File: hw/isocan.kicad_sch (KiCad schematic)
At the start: 10 parts, among them U13 XC6206P332MR, U6 ADUM1201ARZ-RL7, U9 TJA1051TK/3,118

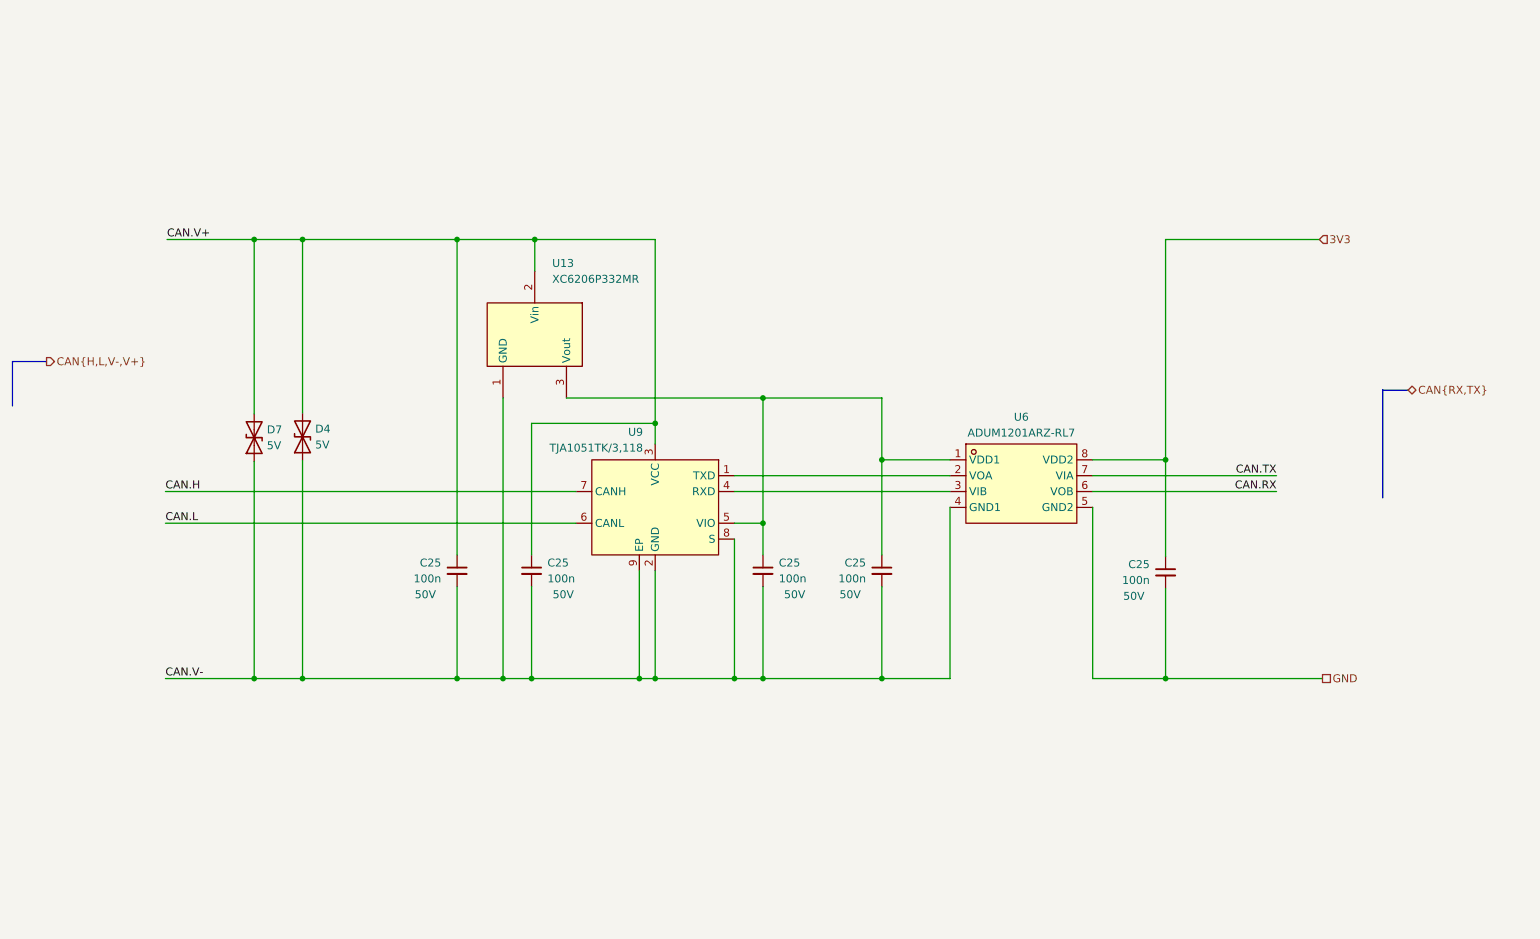
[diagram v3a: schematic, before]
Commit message: [Hw] Simplifying CAN
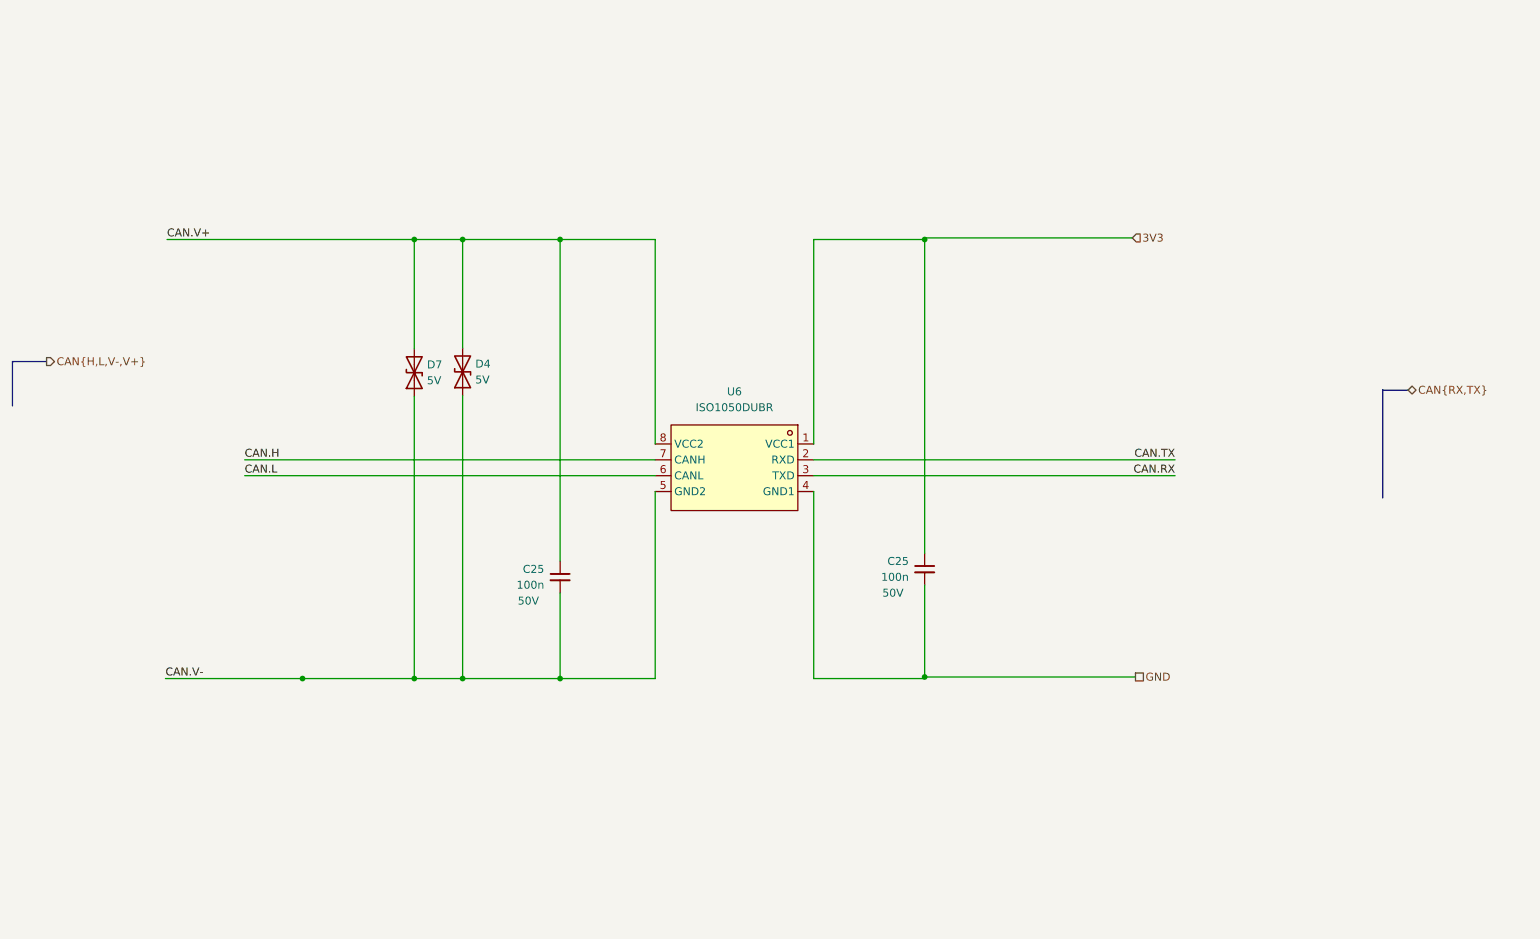
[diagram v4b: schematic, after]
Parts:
- removed C25 (x3): 100n, Capacitor_SMD:C_0402_1005Metric, symbol Device:C_Small
- removed U13: XC6206P332MR, easyeda:SOT-23-3_L2.9-W1.6-P1.90-LS2.8-BR, symbol easyeda:XC6206P332MR
- removed U6: ADUM1201ARZ-RL7, easyeda:SOIC-8_L4.9-W3.9-P1.27-LS6.0-BL, symbol easyeda:ADUM1201ARZ-RL7
- removed U9: TJA1051TK/3,118, easyeda:HVSON-8_L3.0-W3.0-P0.65-BL-EP, symbol easyeda:TJA1051TK_3,118
- added U6: ISO1050DUBR, easyeda:SOIC-8_L9.3-W6.6-P2.54-LS10.4-BL, symbol easyeda:ISO1050DUBR
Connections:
- net 3V3: now also U6.1 (VCC1)
- net CAN.H: now also U6.7 (CANH)
- net CAN.L: now also U6.6 (CANL)
- net CAN.RX: now also U6.3 (TXD)
- net CAN.TX: now also U6.2 (RXD)
- net CAN.V+: now also U6.8 (VCC2)
- net CAN.V-: now also U6.5 (GND2)
- net GND: now also U6.4 (GND1)
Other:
- moved on the sheet: C25, D4, D7

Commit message: [Hw] Small ICs to make 3 wire can possible in this formfactor
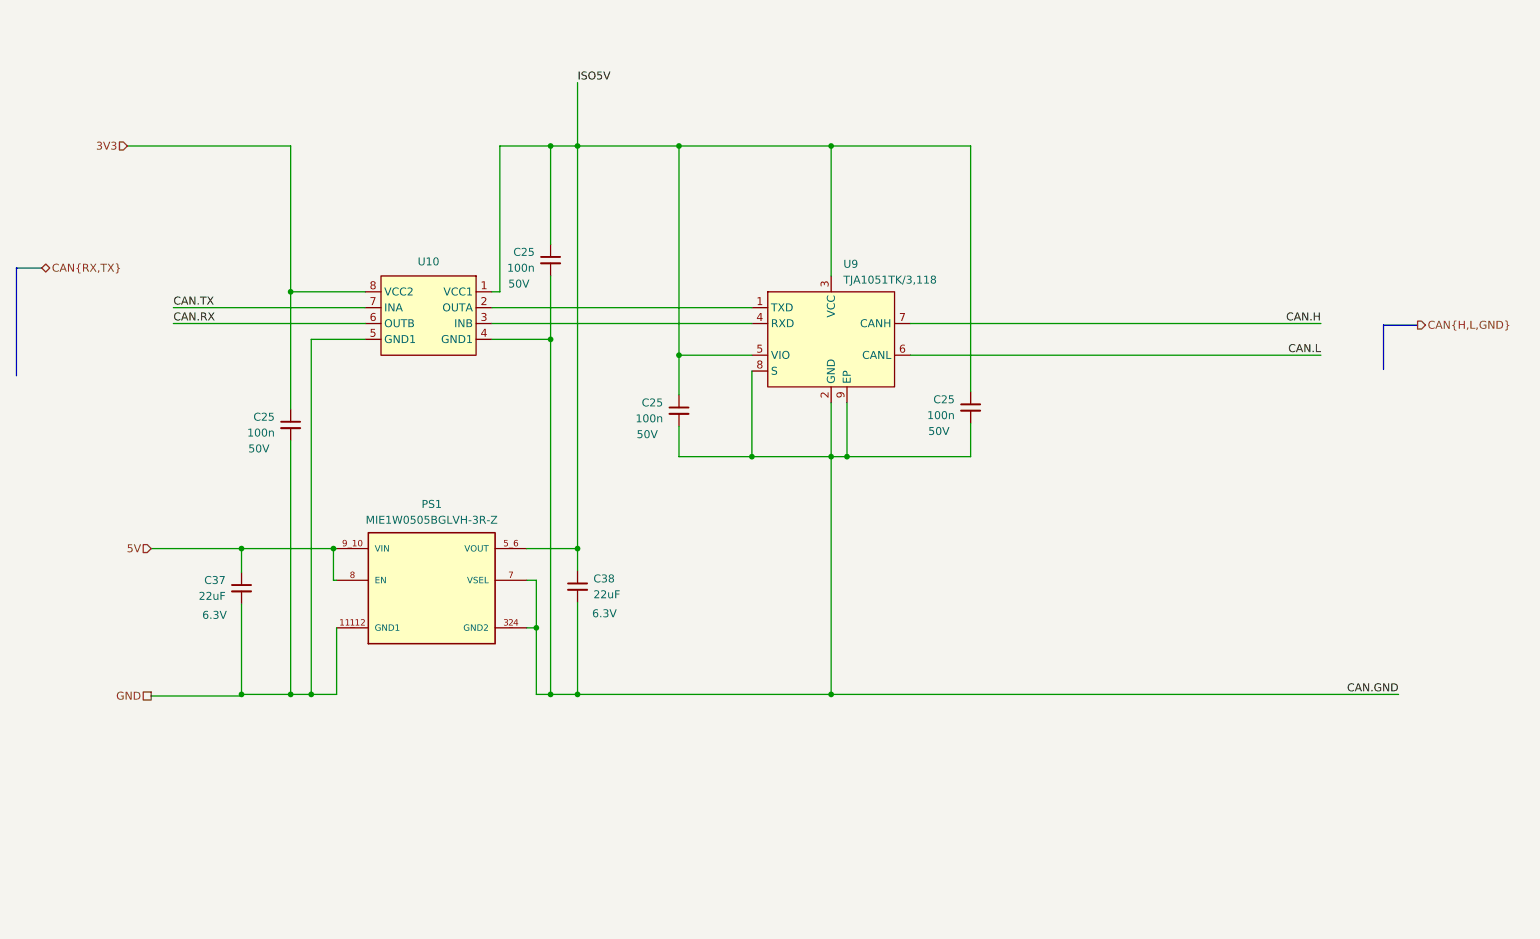
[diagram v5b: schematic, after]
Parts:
- removed C25: 100n, Capacitor_SMD:C_0402_1005Metric, symbol Device:C_Small
- removed D4, D7: 5V, easyeda:X1-DFN1006-2_L1.0-W0.6-RD, symbol Device:D_TVS
- removed U6: ISO1050DUBR, easyeda:SOIC-8_L9.3-W6.6-P2.54-LS10.4-BL, symbol easyeda:ISO1050DUBR
- added C25 (x3): 100n, Capacitor_SMD:C_0402_1005Metric, symbol Device:C_Small
- added C37, C38: 22uF, Capacitor_SMD:C_0402_1005Metric, symbol Device:C_Small
- added PS1: MIE1W0505BGLVH-3R-Z, MIE1W0505BGLVH-3R-Z:CONV_MIE1W0505BGLVH-3R-Z, symbol MIE1W0505BGLVH-3R-Z:MIE1W0505BGLVH-3R-Z
- added U10: ~, Package_DFN_QFN:DFN-8-1EP_3x2mm_P0.5mm_EP1.3x1.5mm, symbol local_lib:ISO6521FREUR
- added U9: TJA1051TK/3,118, easyeda:HVSON-8_L3.0-W3.0-P0.65-BL-EP, symbol easyeda:TJA1051TK_3,118
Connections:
- net 3V3: now also U10.8 (VCC2)
- net CAN.H: now also U9.7 (CANH)
- net CAN.L: now also U9.6 (CANL)
- net CAN.RX: now also U10.6 (OUTB)
- net CAN.TX: now also U10.7 (INA)
- net GND: now also C37.2, PS1.1 (GND1), PS1.11_12 (GND1), U10.5 (GND1)
- new net: U10.2 (OUTA), U9.1 (TXD)
- new net: U10.3 (INB), U9.4 (RXD)
- new net 5V: C37.1, PS1.8 (EN), PS1.9_10 (VIN)
- new net CAN.GND: C25.2, C25.2, C25.2, C38.2, PS1.2 (GND2), PS1.3_4 (GND2), PS1.7 (VSEL), U10.4 (GND1), U9.2 (GND), U9.8 (S), U9.9 (EP)
- new net ISO5V: C25.1, C25.1, C25.1, C38.1, PS1.5_6 (VOUT), U10.1 (VCC1), U9.3 (VCC), U9.5 (VIO)
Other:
- moved on the sheet: C25

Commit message: [Hw] USBC fixes, 3 wire can, encoder and comms headers
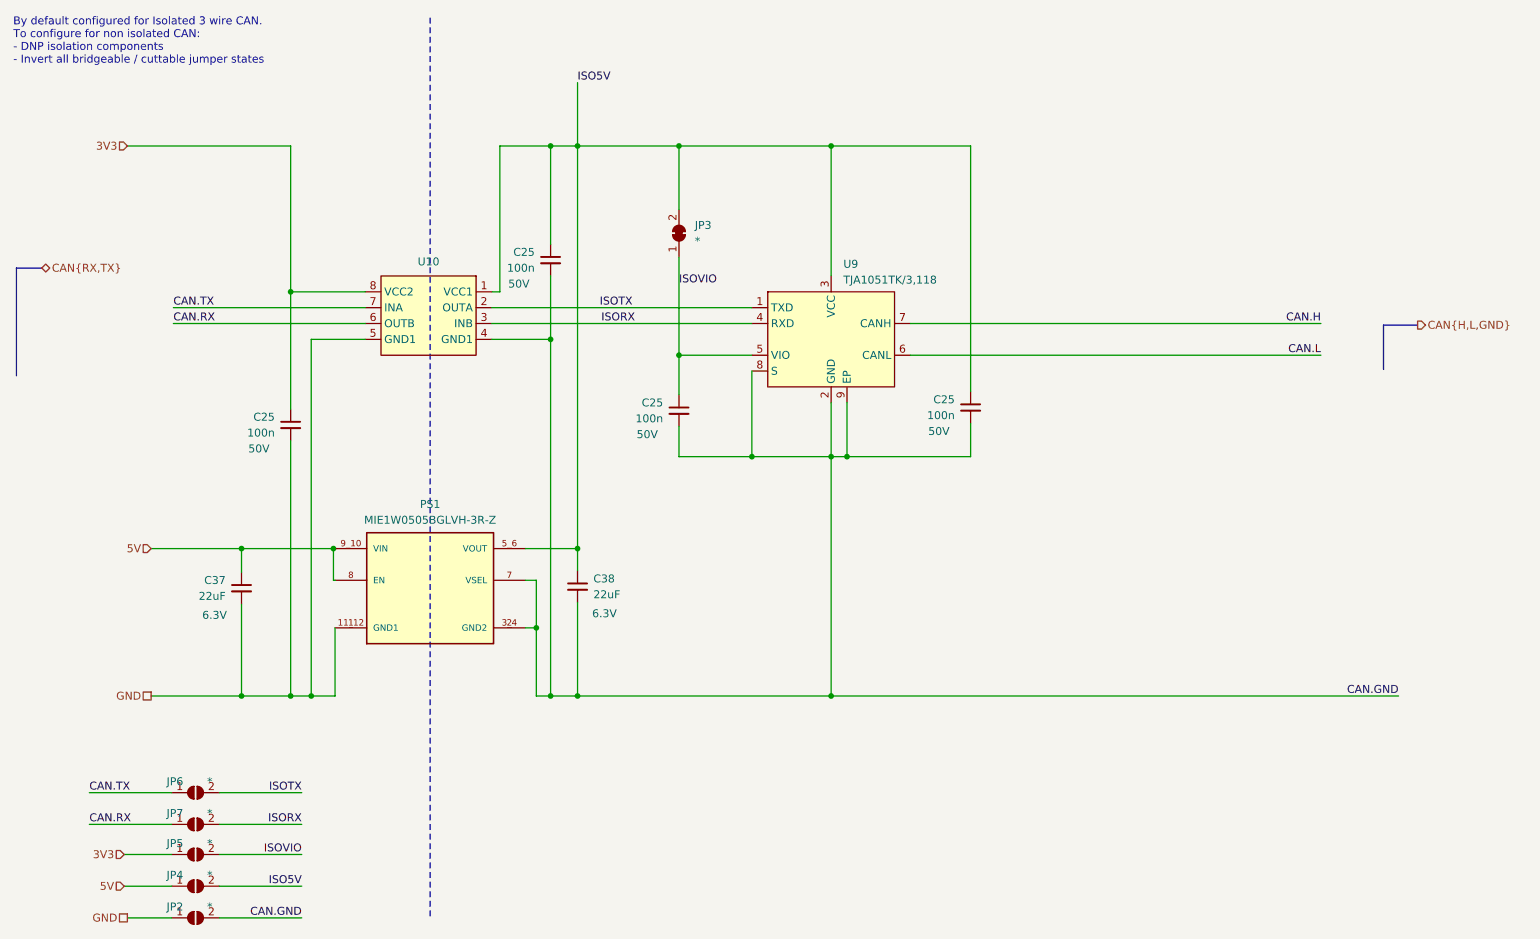
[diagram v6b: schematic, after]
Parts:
- added JP2, JP4, JP5, JP6, JP7: *, Jumper:SolderJumper-2_P1.3mm_Open_RoundedPad1.0x1.5mm, symbol Jumper:SolderJumper_2_Open
- added JP3: *, Jumper:SolderJumper-2_P1.3mm_Bridged_RoundedPad1.0x1.5mm, symbol Jumper:SolderJumper_2_Bridged
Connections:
- net 3V3: now also JP5.1 (A)
- net 5V: now also JP4.1 (A)
- net CAN.GND: now also JP2.2 (B)
- net CAN.RX: now also JP7.1 (A)
- net CAN.TX: now also JP6.1 (A)
- net GND: now also JP2.1 (A)
- net ISO5V: now also JP3.2 (B), JP4.2 (B); no longer C25.1, U9.5 (VIO)
- net ISOTX: now reaches U10.2 (OUTA), U9.1 (TXD)
- net ISOTX: now also JP6.2 (B)
- net ISORX: now reaches U10.3 (INB), U9.4 (RXD)
- net ISORX: now also JP7.2 (B)
- new net ISOVIO: C25.1, JP3.1 (A), JP5.2 (B), U9.5 (VIO)
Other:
- note added: "By default configured for Isolated 3 wire CAN. To configure for non isolated CAN: - DNP isolation components - Invert all bridgeable / cuttable jumper states"

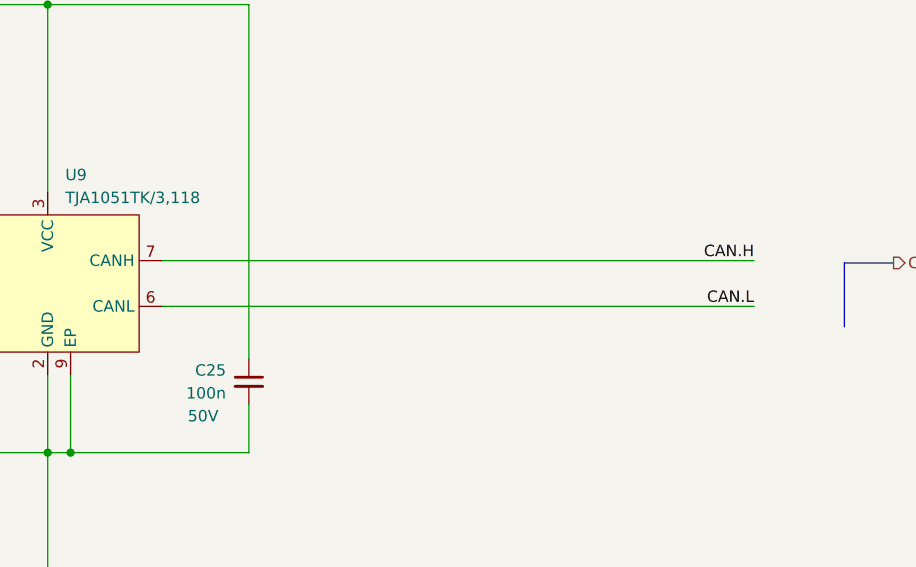
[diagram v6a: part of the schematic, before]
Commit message: [Hw] Optimised pin out for routing, new layout
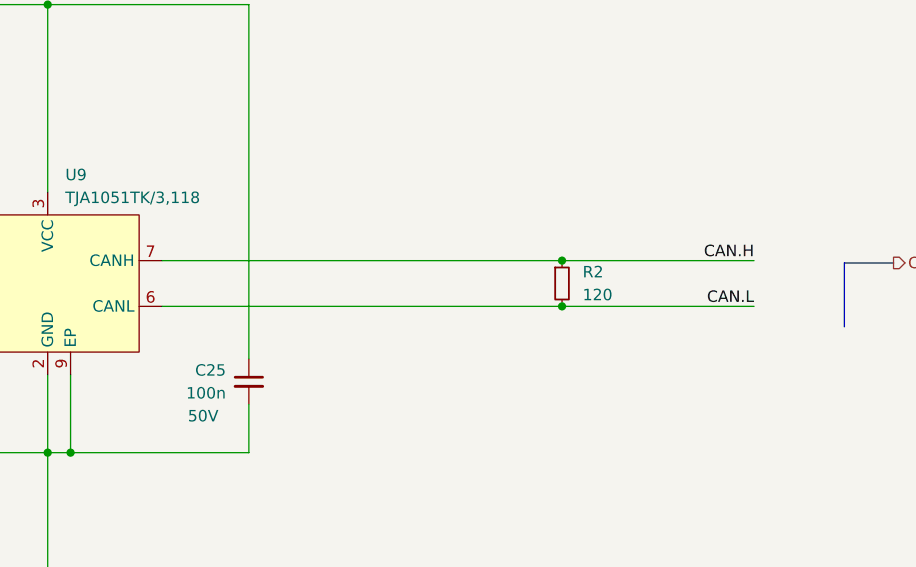
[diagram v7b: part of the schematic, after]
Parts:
- added R2: 120, Resistor_SMD:R_0603_1608Metric, symbol Device:R_Small
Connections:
- net CAN.H: now also R2.1
- net CAN.L: now also R2.2
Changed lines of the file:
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@@
   (junction (at 115.316 134.874) (diameter 0) (color 0 0 0 0)
   )
+  (junction (at 217.424 80.264) (diameter 0) (color 0 0 0 0)
+  )
   (junction (at 73.66 70.104) (diameter 0) (color 0 0 0 0)
   )
@@
   (junction (at 160.274 46.736) (diameter 0) (color 0 0 0 0)
   )
+  (junction (at 217.424 75.184) (diameter 0) (color 0 0 0 0)
+  )
   (junction (at 115.316 77.724) (diameter 0) (color 0 0 0 0)
   )
@@
     (stroke (width 0) (type default))
   )
-  (wire (pts (xy 238.76 75.184) (xy 172.974 75.184))
+  (wire (pts (xy 238.76 75.184) (xy 217.424 75.184))
     (stroke (width 0) (type default))
   )
@@
     (stroke (width 0) (type default))
   )
+  (wire (pts (xy 217.424 75.184) (xy 172.974 75.184))
+    (stroke (width 0) (type default))
+  )
   (wire (pts (xy 147.574 96.52) (xy 135.89 96.52))
     (stroke (width 0) (type default))
@@
     (stroke (width 0) (type default))
   )
+  (wire (pts (xy 217.424 80.264) (xy 172.974 80.264))
+    (stroke (width 0) (type default))
+  )
   (wire (pts (xy 105.918 77.724) (xy 115.316 77.724))
     (stroke (width 0) (type default))
@@
     (stroke (width 0) (type default))
   )
-  (wire (pts (xy 238.76 80.264) (xy 172.974 80.264))
+  (wire (pts (xy 238.76 80.264) (xy 217.424 80.264))
     (stroke (width 0) (type default))
   )
@@
         )
       )
+    )
+  )
+  (symbol (lib_id "Device:R_Small") (at 217.424 77.724 0) (unit 1)
+    (in_bom yes) (on_board yes) (dnp no) (fields_autoplaced)
+    (property "Reference" "R2" (at 219.71 76.454 0)
+      (effects (font (size 1.27 1.27)) (justify left))
+    )
+    (property "Value" "120" (at 219.71 78.994 0)
+      (effects (font (size 1.27 1.27)) (justify left))
+    )
+    (property "Footprint" "Resistor_SMD:R_0603_1608Metric" (at 217.424 77.724 0)
+      (effects (font (size 1.27 1.27)) hide)
+    )
+    (property "Datasheet" "~" (at 217.424 77.724 0)
+      (effects (font (size 1.27 1.27)) hide)
+    )
+    (pin "1")
+    (pin "2")
+    (instances
+      (project "foc8313"
+        (path "/6a0f293a-1ae1-497a-a3c1-0d8f9e6f81b9/67c38edc-7843-4b4c-b50a-94fd700c0fa2"
+          (reference "R2") (unit 1)
+        )
+      )

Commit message: [Hw] Routing topology complete
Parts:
- JP2, JP4, JP5, JP6, JP7: footprint Jumper:SolderJumper-2_P1.3mm_Open_RoundedPad1.0x1.5mm -> local_lib:jumper12_open
- JP3: footprint Jumper:SolderJumper-2_P1.3mm_Bridged_RoundedPad1.0x1.5mm -> local_lib:jumper12_closed
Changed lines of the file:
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@@
       (effects (font (size 1.27 1.27)))
     )
-    (property "Footprint" "Jumper:SolderJumper-2_P1.3mm_Open_RoundedPad1.0x1.5mm" (at 58.42 150.368 0)
+    (property "Footprint" "local_lib:jumper12_open" (at 58.42 150.368 0)
       (effects (font (size 1.27 1.27)) hide)
     )
@@
       (effects (font (size 1.27 1.27)))
     )
-    (property "Footprint" "Jumper:SolderJumper-2_P1.3mm_Open_RoundedPad1.0x1.5mm" (at 58.42 155.448 0)
+    (property "Footprint" "local_lib:jumper12_open" (at 58.42 155.448 0)
       (effects (font (size 1.27 1.27)) hide)
     )
@@
       (effects (font (size 1.27 1.27)) (justify right))
     )
-    (property "Footprint" "Jumper:SolderJumper-2_P1.3mm_Bridged_RoundedPad1.0x1.5mm" (at 135.89 60.706 0)
+    (property "Footprint" "local_lib:jumper12_closed" (at 135.89 60.706 0)
       (effects (font (size 1.27 1.27)) hide)
     )
@@
       (effects (font (size 1.27 1.27)))
     )
-    (property "Footprint" "Jumper:SolderJumper-2_P1.3mm_Open_RoundedPad1.0x1.5mm" (at 58.42 170.434 0)
+    (property "Footprint" "local_lib:jumper12_open" (at 58.42 170.434 0)
       (effects (font (size 1.27 1.27)) hide)
     )
@@
       (effects (font (size 1.27 1.27)))
     )
-    (property "Footprint" "Jumper:SolderJumper-2_P1.3mm_Open_RoundedPad1.0x1.5mm" (at 58.42 160.274 0)
+    (property "Footprint" "local_lib:jumper12_open" (at 58.42 160.274 0)
       (effects (font (size 1.27 1.27)) hide)
     )
@@
       (effects (font (size 1.27 1.27)))
     )
-    (property "Footprint" "Jumper:SolderJumper-2_P1.3mm_Open_RoundedPad1.0x1.5mm" (at 58.42 165.354 0)
-      (effects (font (size 1.27 1.27)) hide)
-    )
+    (property "Footprint" "local_lib:jumper12_open" (at 58.42 165.354 0)
+      (effects (font (size 1.27 1.27)) hide)
+    )
